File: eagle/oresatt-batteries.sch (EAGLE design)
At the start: 62 parts, among them IC1 74AHC1G08DBV, U1 TCAN330, U2 STM32F042K6, X1 16MHz

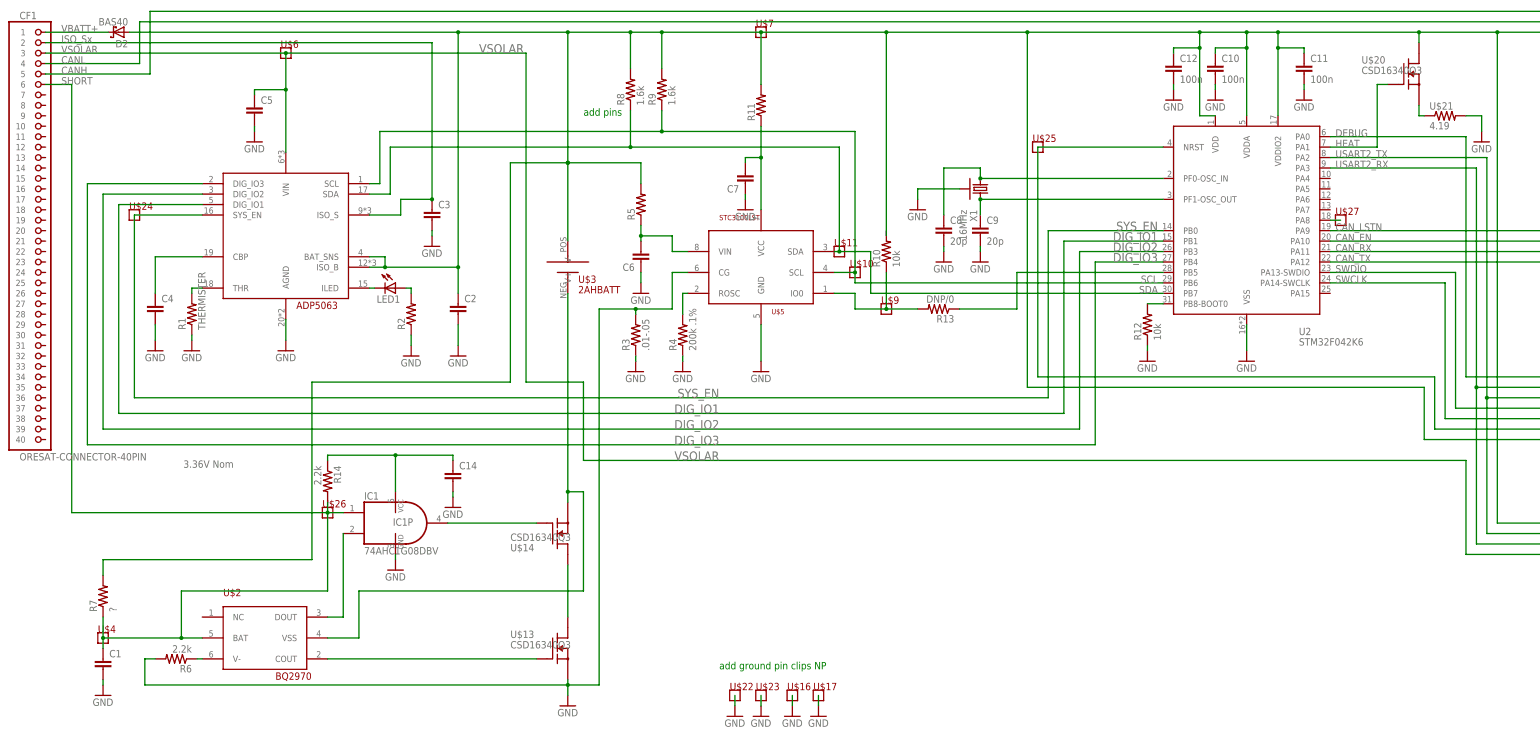
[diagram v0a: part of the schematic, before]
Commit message: Cleaned up schematic, moved STC sense resistor to proper place.
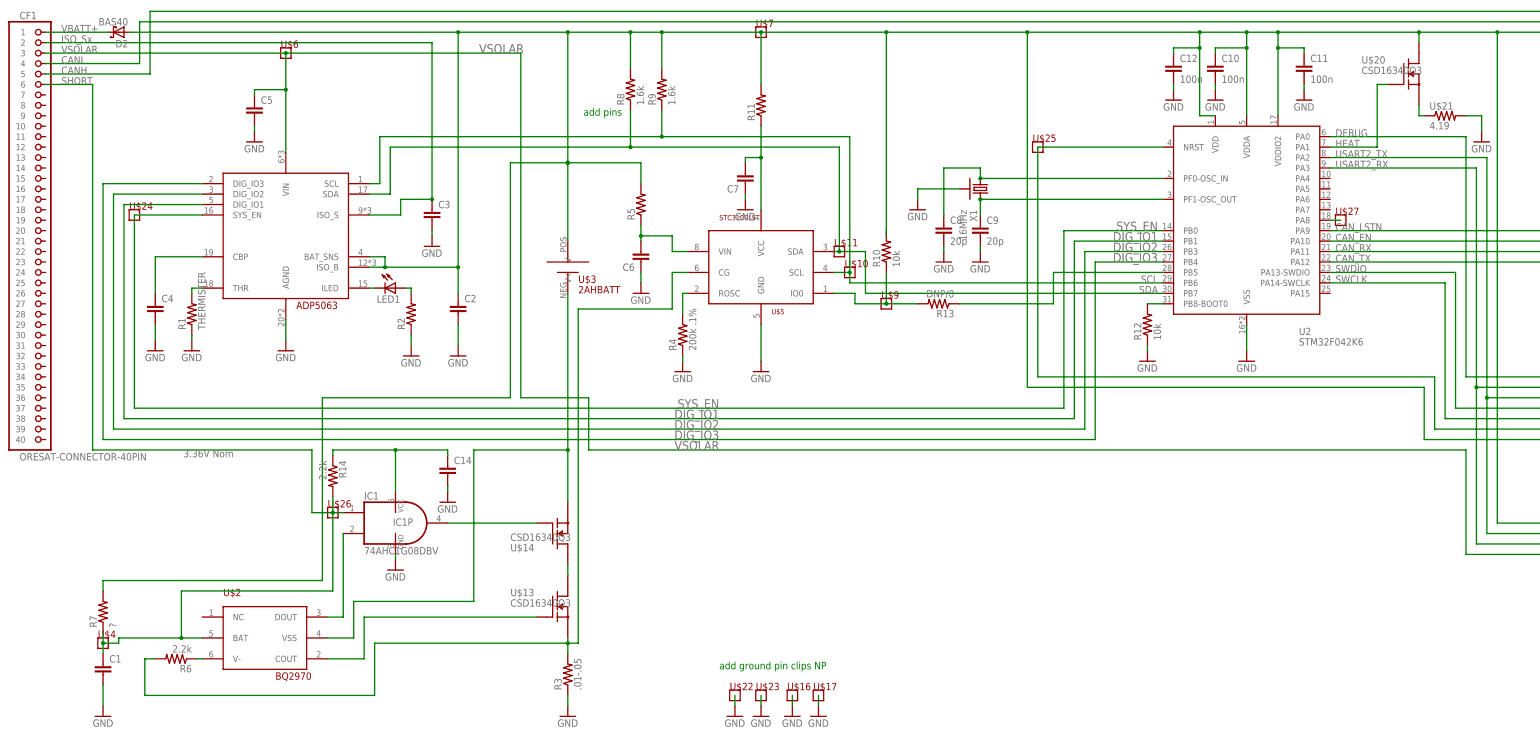
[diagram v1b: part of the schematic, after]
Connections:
- net N$3 renamed ANDDRIVE
- new net C_SENSE: R3.2, R6.2, U$13.S, U$5.CG
- net GND: no longer R3.2, R6.2, U$13.S, U$5.CG
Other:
- moved on the sheet: C1, C14, R13, R14, R3, R7, U$10, U$13, U$26, U$4, U$9

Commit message: Schematic Cleanup, added labels and isolated chips visually
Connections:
- net VBATT+: now also R10.2
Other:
- note added: "Battery Charger"
- note added: "Breakout Pins"
- note added: "CAN Transciever"
- note added: "Cell Protection"
- note added: "Fuel Gauge"
- note added: "Ground Pins"
- note added: "LiPo Cell"
- note added: "STM Microcontroller"
- moved on the sheet: C1, C10, C11, C12, C13, C14, C6, C7, C8, C9, CF1, CF2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
